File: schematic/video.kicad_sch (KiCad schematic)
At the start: 14 parts, among them J1 Conn_Coaxial, Q1 2N3904, U1 TMS4416, U14 TMS9118NL, U3 TMS4416, Y1 Crystal

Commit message: bootup works, controller waits, but no response
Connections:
- net D0: now also U14.17 (CD7); no longer U14.24 (CD0)
- net D1: now also U14.18 (CD6); no longer U14.23 (CD1)
- net D2: now also U14.19 (CD5); no longer U14.22 (CD2)
- net D3: now also U14.20 (CD4); no longer U14.21 (CD3)
- net D4: now also U14.21 (CD3); no longer U14.20 (CD4)
- net D5: now also U14.22 (CD2); no longer U14.19 (CD5)
- net D6: now also U14.23 (CD1); no longer U14.18 (CD6)
- net D7: now also U14.24 (CD0); no longer U14.17 (CD7)

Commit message: update pdf schematic and schematic wording
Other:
- title: Righteous Tentacle, Colecovision Reverse Engineering Project -> Mini Colecovision
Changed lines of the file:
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@@
   (paper "USLetter")
   (title_block
-    (title "Righteous Tentacle, Colecovision Reverse Engineering Project")
-    (date "2023-06-18")
-    (rev "1.0.0.F")
+    (title "Mini Colecovision")
+    (date "2024-03-25")
+    (rev "1.0.0")
     (company "sparkletron")
     (comment 1 "Jay Convertino")
     (comment 2 "MIT LICENSE")
-    (comment 3 "PCB: 75743 REV F")
+    (comment 3 "TARGET: Portable")
   )
   (junction (at 114.554 164.338) (diameter 0) (color 0 0 0 0)

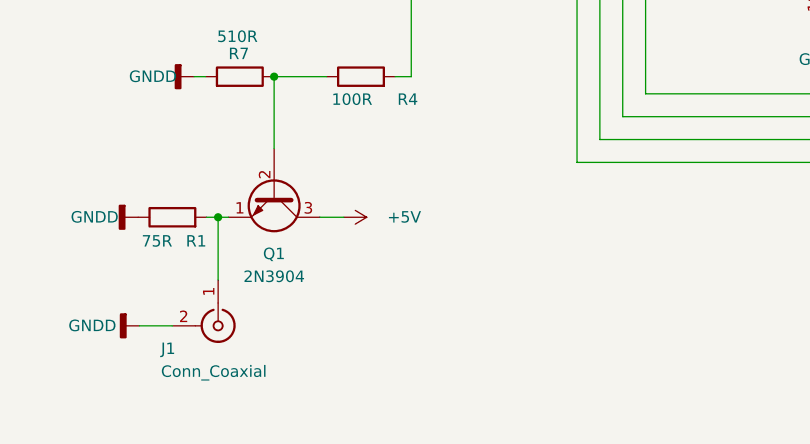
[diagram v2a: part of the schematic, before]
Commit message: first commit with PCB revised for super game module. Needs model updates and tweaks
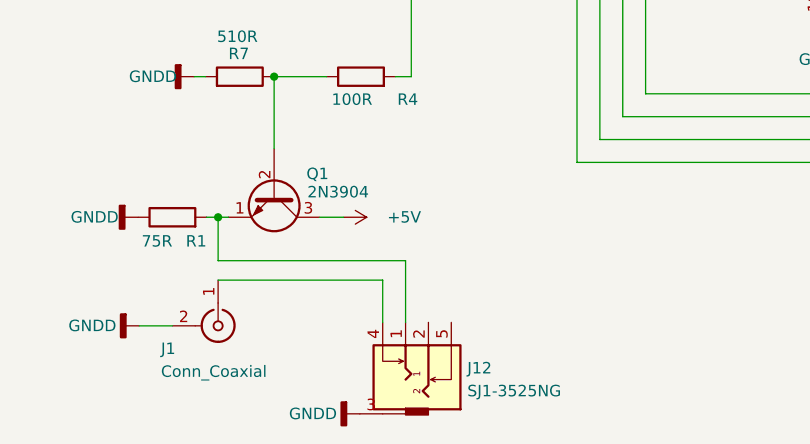
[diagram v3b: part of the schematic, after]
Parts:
- added J12: SJ1-3525NG, jacks:spc21348, symbol jacks:eighth_inch_jack
- U1, U3: footprint Package_DIP:DIP-18_W7.62mm_LongPads -> Package_DIP:DIP-18_W7.62mm
- U14: footprint Package_DIP:DIP-40_W15.24mm_LongPads -> Package_DIP:DIP-40_W15.24mm
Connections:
- net GNDD: now also J12.3
- net at Q1.1 (E), R1.2: now also J12.1; no longer J1.1 (In)
- new net: J1.1 (In), J12.4
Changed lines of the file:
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@@
     (comment 3 "TARGET: Portable")
   )
+  (junction (at 53.975 90.043) (diameter 0) (color 0 0 0 0)
+  )
+  (junction (at 53.975 97.663) (diameter 0) (color 0 0 0 0)
+  )
   (junction (at 114.554 164.338) (diameter 0) (color 0 0 0 0)
-  )
-  (junction (at 53.975 90.043) (diameter 0) (color 0 0 0 0)
-  )
-  (junction (at 53.975 97.663) (diameter 0) (color 0 0 0 0)
   )
   (junction (at 42.545 90.043) (diameter 0) (color 0 0 0 0)
@@
     (stroke (width 0) (type default))
   )
-  (wire (pts (xy 114.554 164.338) (xy 114.554 171.323))
-    (stroke (width 0) (type default))
-  )
   (wire (pts (xy 120.777 148.717) (xy 120.777 156.718))
     (stroke (width 0) (type default))
@@
     (stroke (width 0) (type default))
   )
+  (wire (pts (xy 114.554 164.338) (xy 115.697 164.338))
+    (stroke (width 0) (type default))
+  )
   (bus (pts (xy 198.247 73.787) (xy 198.247 76.327))
     (stroke (width 0) (type default))
@@
     (stroke (width 0) (type default))
   )
-  (wire (pts (xy 114.554 164.338) (xy 115.697 164.338))
-    (stroke (width 0) (type default))
-  )
   (wire (pts (xy 136.017 62.992) (xy 162.052 62.992))
     (stroke (width 0) (type default))
@@
     (stroke (width 0) (type default))
   )
+  (wire (pts (xy 135.382 169.164) (xy 135.382 176.022))
+    (stroke (width 0) (type default))
+  )
   (wire (pts (xy 136.017 112.522) (xy 159.512 112.522))
     (stroke (width 0) (type default))
   )
+  (wire (pts (xy 114.554 164.338) (xy 114.554 169.164))
+    (stroke (width 0) (type default))
+  )
   (bus (pts (xy 141.097 82.042) (xy 141.097 84.582))
     (stroke (width 0) (type default))
@@
     (stroke (width 0) (type default))
   )
+  (wire (pts (xy 114.554 169.164) (xy 135.382 169.164))
+    (stroke (width 0) (type default))
+  )
   (wire (pts (xy 193.802 150.622) (xy 193.802 137.922))
     (stroke (width 0) (type default))
@@
     (stroke (width 0) (type default))
   )
+  (wire (pts (xy 132.842 171.323) (xy 132.842 176.022))
+    (stroke (width 0) (type default))
+  )
   (wire (pts (xy 105.537 116.332) (xy 105.537 117.602))
     (stroke (width 0) (type default))
@@
   )
   (wire (pts (xy 92.837 108.712) (xy 92.837 112.522))
+    (stroke (width 0) (type default))
+  )
+  (wire (pts (xy 132.842 171.323) (xy 114.554 171.323))
     (stroke (width 0) (type default))
   )
@@
     (effects (font (size 1.27 1.27)) (justify left))
   )
+  (symbol (lib_id "jacks:eighth_inch_jack") (at 130.302 182.372 270) (mirror x) (unit 1)
+    (in_bom yes) (on_board yes) (dnp no) (fields_autoplaced)
+    (property "Reference" "J12" (at 142.24 181.102 90)
+      (effects (font (size 1.27 1.27)) (justify left))
+    )
+    (property "Value" "SJ1-3525NG" (at 142.24 183.642 90)
+      (effects (font (size 1.27 1.27)) (justify left))
+    )
+    (property "Footprint" "jacks:spc21348" (at 130.302 182.372 0)
+      (effects (font (size 1.27 1.27)) hide)
+    )
+    (property "Datasheet" "" (at 130.302 182.372 0)
+      (effects (font (size 1.27 1.27)) hide)
+    )
+    (pin "2")
+    (pin "5")
+    (pin "4")
+    (pin "3")
+    (pin "1")
+    (instances
+      (project "coleco_original"
+        (path "/970e0f64-111f-41e3-9f5a-fb0d0f6fa101/00000000-0000-0000-0000-00006262475e"
+          (reference "J12") (unit 1)
+        )
+      )
+    )
+  )
   (symbol (lib_id "Transistor_BJT:2N3904") (at 120.777 161.798 270) (unit 1)
-    (in_bom yes) (on_board yes) (dnp no) (fields_autoplaced)
-    (property "Reference" "Q1" (at 120.777 168.402 90)
+    (in_bom yes) (on_board yes) (dnp no)
+    (property "Reference" "Q1" (at 125.603 159.512 90)
       (effects (font (size 1.27 1.27)))
     )
-    (property "Value" "2N3904" (at 120.777 170.942 90)
+    (property "Value" "2N3904" (at 127.889 161.544 90)
       (effects (font (size 1.27 1.27)))
     )
@@
       (effects (font (size 1.27 1.27)) (justify left))
     )
-    (property "Footprint" "Package_DIP:DIP-40_W15.24mm_LongPads" (at 123.317 60.452 0)
+    (property "Footprint" "Package_DIP:DIP-40_W15.24mm" (at 123.317 60.452 0)
       (effects (font (size 1.27 1.27)) hide)
     )
@@
     )
   )
+  (symbol (lib_id "power:GNDD") (at 130.302 186.182 270) (unit 1)
+    (in_bom yes) (on_board yes) (dnp no) (fields_autoplaced)
+    (property "Reference" "#PWR085" (at 123.952 186.182 0)
+      (effects (font (size 1.27 1.27)) hide)
+    )
+    (property "Value" "GNDD" (at 127.762 186.182 90)
+      (effects (font (size 1.27 1.27)) (justify right))
+    )
+    (property "Footprint" "" (at 130.302 186.182 0)
+      (effects (font (size 1.27 1.27)) hide)
+    )
+    (property "Datasheet" "" (at 130.302 186.182 0)
+      (effects (font (size 1.27 1.27)) hide)
+    )
+    (pin "1")
+    (instances
+      (project "coleco_original"
+        (path "/970e0f64-111f-41e3-9f5a-fb0d0f6fa101/00000000-0000-0000-0000-00006262475e"
+          (reference "#PWR085") (unit 1)
+        )
+      )
+    )
+  )
   (symbol (lib_id "Device:R") (at 109.474 164.338 90) (unit 1)
     (in_bom yes) (on_board yes) (dnp no)
@@
       (effects (font (size 1.27 1.27)) (justify left))
     )
-    (property "Footprint" "Package_DIP:DIP-18_W7.62mm_LongPads" (at 181.737 103.632 0)
+    (property "Footprint" "Package_DIP:DIP-18_W7.62mm" (at 181.737 103.632 0)
       (effects (font (size 1.27 1.27)) hide)
     )
@@
       (effects (font (size 1.27 1.27)) (justify left))
     )
-    (property "Footprint" "Package_DIP:DIP-18_W7.62mm_LongPads" (at 181.737 72.517 0)
-      (effects (font (size 1.27 1.27)) hide)
-    )
+    (property "Footprint" "Package_DIP:DIP-18_W7.62mm" (at 181.737 72.517 0)
+      (effects (font (size 1.27 1.27)) hide)
+    )

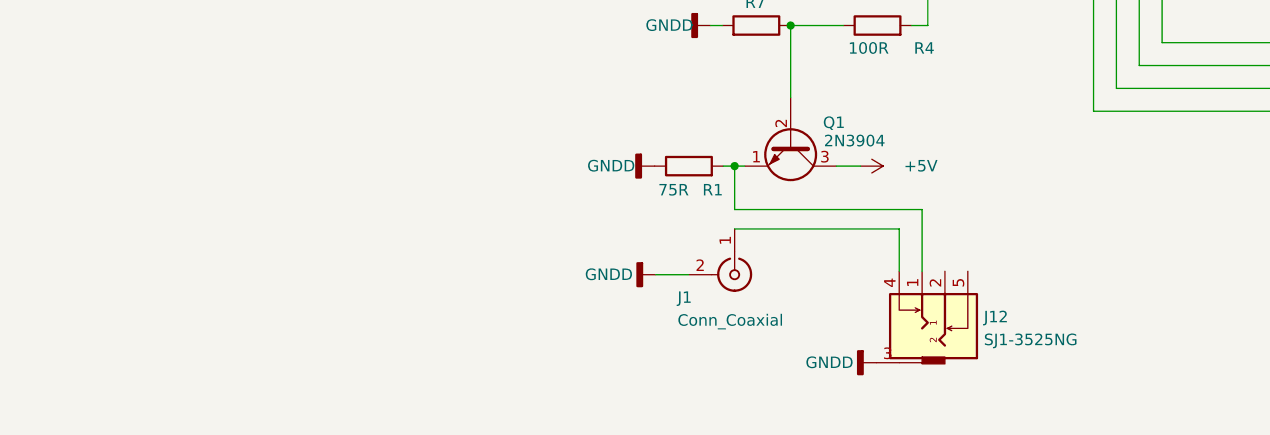
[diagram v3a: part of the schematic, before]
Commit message: updated output jacks to correct footprint
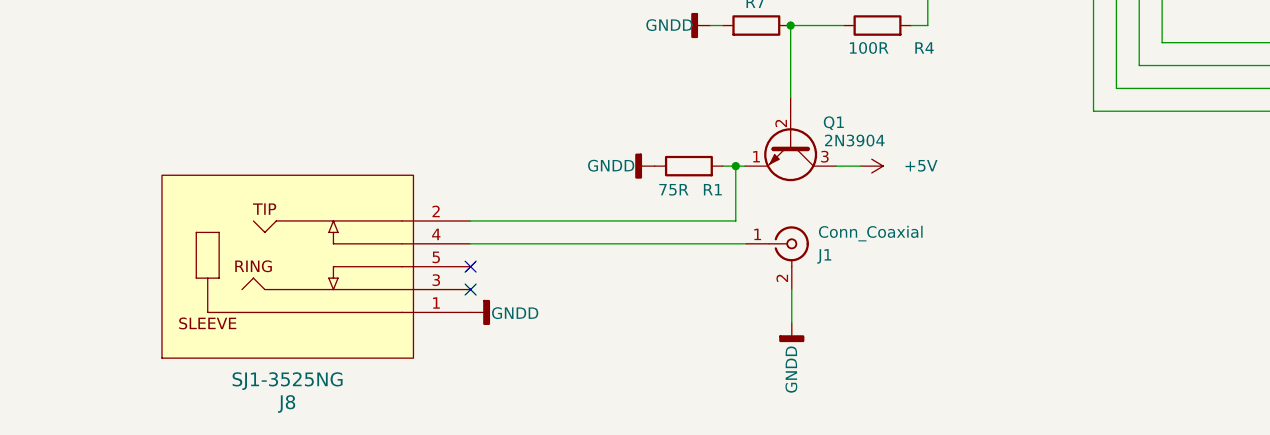
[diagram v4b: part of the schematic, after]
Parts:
- removed J12: SJ1-3525NG, jacks:spc21348, symbol jacks:eighth_inch_jack
- added J8: SJ1-3525NG, jacks2:SJ1-3525NG_CUD, symbol SJ-63053A:SJ1-3525NG
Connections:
- net GNDD: now also J8.1
- net at Q1.1 (E), R1.2: now also J8.2
- net at J1.1 (In): now also J8.4
- no-connect marks 2 -> 4
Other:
- moved on the sheet: J1
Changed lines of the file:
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@@
   (junction (at 53.975 97.663) (diameter 0) (color 0 0 0 0)
   )
-  (junction (at 114.554 164.338) (diameter 0) (color 0 0 0 0)
-  )
   (junction (at 42.545 90.043) (diameter 0) (color 0 0 0 0)
   )
@@
   (junction (at 164.592 98.552) (diameter 0) (color 0 0 0 0)
   )
+  (junction (at 114.681 164.338) (diameter 0) (color 0 0 0 0)
+  )
   (junction (at 105.537 117.602) (diameter 0) (color 0 0 0 0)
   )
@@
   (junction (at 198.247 87.122) (diameter 0) (color 0 0 0 0)
   )
+  (no_connect (at 85.217 175.514))
   (no_connect (at 136.017 122.682))
   (no_connect (at 110.617 122.682))
+  (no_connect (at 85.217 178.054))
   (bus_entry (at 195.707 104.902) (size 2.54 -2.54)
     (stroke (width 0) (type default))
@@
     (stroke (width 0) (type default))
   )
-  (wire (pts (xy 113.284 164.338) (xy 114.554 164.338))
-    (stroke (width 0) (type default))
-  )
-  (wire (pts (xy 114.554 164.338) (xy 115.697 164.338))
+  (wire (pts (xy 113.284 164.338) (xy 114.681 164.338))
     (stroke (width 0) (type default))
   )
@@
     (stroke (width 0) (type default))
   )
+  (wire (pts (xy 114.681 164.338) (xy 115.697 164.338))
+    (stroke (width 0) (type default))
+  )
   (bus (pts (xy 198.247 99.822) (xy 198.247 102.362))
     (stroke (width 0) (type default))
@@
     (stroke (width 0) (type default))
   )
-  (wire (pts (xy 135.382 169.164) (xy 135.382 176.022))
-    (stroke (width 0) (type default))
-  )
   (wire (pts (xy 136.017 112.522) (xy 159.512 112.522))
     (stroke (width 0) (type default))
   )
-  (wire (pts (xy 114.554 164.338) (xy 114.554 169.164))
+  (wire (pts (xy 114.681 164.338) (xy 114.681 170.434))
     (stroke (width 0) (type default))
   )
@@
     (stroke (width 0) (type default))
   )
-  (wire (pts (xy 114.554 169.164) (xy 135.382 169.164))
+  (wire (pts (xy 85.217 170.434) (xy 114.681 170.434))
     (stroke (width 0) (type default))
   )
@@
     (stroke (width 0) (type default))
   )
-  (wire (pts (xy 132.842 171.323) (xy 132.842 176.022))
-    (stroke (width 0) (type default))
-  )
   (wire (pts (xy 105.537 116.332) (xy 105.537 117.602))
     (stroke (width 0) (type default))
@@
     (stroke (width 0) (type default))
   )
+  (wire (pts (xy 85.217 172.974) (xy 115.824 172.974))
+    (stroke (width 0) (type default))
+  )
   (wire (pts (xy 134.239 148.717) (xy 136.017 148.717))
     (stroke (width 0) (type default))
@@
     (stroke (width 0) (type default))
   )
-  (wire (pts (xy 132.842 171.323) (xy 114.554 171.323))
-    (stroke (width 0) (type default))
-  )
   (wire (pts (xy 195.707 38.227) (xy 191.897 38.227))
     (stroke (width 0) (type default))
@@
     (stroke (width 0) (type default))
   )
-  (wire (pts (xy 105.791 176.403) (xy 109.474 176.403))
+  (wire (pts (xy 120.904 181.737) (xy 120.904 178.054))
     (stroke (width 0) (type default))
   )
@@
   (hierarchical_label "CLK" (shape output) (at 139.827 125.222 0) (fields_autoplaced)
     (effects (font (size 1.27 1.27)) (justify left))
-  )
-  (symbol (lib_id "jacks:eighth_inch_jack") (at 130.302 182.372 270) (mirror x) (unit 1)
-    (in_bom yes) (on_board yes) (dnp no) (fields_autoplaced)
-    (property "Reference" "J12" (at 142.24 181.102 90)
-      (effects (font (size 1.27 1.27)) (justify left))
-    )
-    (property "Value" "SJ1-3525NG" (at 142.24 183.642 90)
-      (effects (font (size 1.27 1.27)) (justify left))
-    )
-    (property "Footprint" "jacks:spc21348" (at 130.302 182.372 0)
-      (effects (font (size 1.27 1.27)) hide)
-    )
-    (property "Datasheet" "" (at 130.302 182.372 0)
-      (effects (font (size 1.27 1.27)) hide)
-    )
-    (pin "2")
-    (pin "5")
-    (pin "4")
-    (pin "3")
-    (pin "1")
-    (instances
-      (project "coleco_original"
-        (path "/970e0f64-111f-41e3-9f5a-fb0d0f6fa101/00000000-0000-0000-0000-00006262475e"
-          (reference "J12") (unit 1)
-        )
-      )
-    )
   )
   (symbol (lib_id "Transistor_BJT:2N3904") (at 120.777 161.798 270) (unit 1)
@@
     )
   )
-  (symbol (lib_id "power:GNDD") (at 130.302 186.182 270) (unit 1)
-    (in_bom yes) (on_board yes) (dnp no) (fields_autoplaced)
-    (property "Reference" "#PWR085" (at 123.952 186.182 0)
-      (effects (font (size 1.27 1.27)) hide)
-    )
-    (property "Value" "GNDD" (at 127.762 186.182 90)
+  (symbol (lib_id "power:GNDD") (at 85.217 180.594 90) (mirror x) (unit 1)
+    (in_bom yes) (on_board yes) (dnp no)
+    (property "Reference" "#PWR085" (at 91.567 180.594 0)
+      (effects (font (size 1.27 1.27)) hide)
+    )
+    (property "Value" "GNDD" (at 87.503 180.721 90)
       (effects (font (size 1.27 1.27)) (justify right))
     )
-    (property "Footprint" "" (at 130.302 186.182 0)
-      (effects (font (size 1.27 1.27)) hide)
-    )
-    (property "Datasheet" "" (at 130.302 186.182 0)
+    (property "Footprint" "" (at 85.217 180.594 0)
+      (effects (font (size 1.27 1.27)) hide)
+    )
+    (property "Datasheet" "" (at 85.217 180.594 0)
       (effects (font (size 1.27 1.27)) hide)
     )
@@
     )
   )
+  (symbol (lib_id "SJ-63053A:SJ1-3525NG") (at 85.217 180.594 0) (mirror x) (unit 1)
+    (in_bom yes) (on_board yes) (dnp no) (fields_autoplaced)
+    (property "Reference" "J8" (at 64.897 190.627 0)
+      (effects (font (size 1.524 1.524)))
+    )
+    (property "Value" "SJ1-3525NG" (at 64.897 188.087 0)
+      (effects (font (size 1.524 1.524)))
+    )
+    (property "Footprint" "jacks2:SJ1-3525NG_CUD" (at 85.217 180.594 0)
+      (effects (font (size 1.27 1.27) italic) hide)
+    )
+    (property "Datasheet" "SJ1-3525NG" (at 85.217 180.594 0)
+      (effects (font (size 1.27 1.27) italic) hide)
+    )
+    (pin "2")
+    (pin "3")
+    (pin "5")
+    (pin "4")
+    (pin "1")
+    (instances
+      (project "coleco_original"
+        (path "/970e0f64-111f-41e3-9f5a-fb0d0f6fa101/00000000-0000-0000-0000-00006262475e"
+          (reference "J8") (unit 1)
+        )
+      )
+    )
+  )
   (symbol (lib_id "power:GNDD") (at 105.664 164.338 270) (unit 1)
     (in_bom yes) (on_board yes) (dnp no) (fields_autoplaced)
@@
     )
   )
-  (symbol (lib_id "power:GNDD") (at 105.791 176.403 270) (unit 1)
+  (symbol (lib_id "power:GNDD") (at 120.904 181.737 0) (unit 1)
     (in_bom yes) (on_board yes) (dnp no) (fields_autoplaced)
-    (property "Reference" "#PWR038" (at 99.441 176.403 0)
-      (effects (font (size 1.27 1.27)) hide)
-    )
-    (property "Value" "GNDD" (at 103.251 176.403 90)
+    (property "Reference" "#PWR038" (at 120.904 188.087 0)
+      (effects (font (size 1.27 1.27)) hide)
+    )
+    (property "Value" "GNDD" (at 120.904 184.277 90)
       (effects (font (size 1.27 1.27)) (justify right))
     )
-    (property "Footprint" "" (at 105.791 176.403 0)
-      (effects (font (size 1.27 1.27)) hide)
-    )
-    (property "Datasheet" "" (at 105.791 176.403 0)
+    (property "Footprint" "" (at 120.904 181.737 0)
+      (effects (font (size 1.27 1.27)) hide)
+    )
+    (property "Datasheet" "" (at 120.904 181.737 0)
       (effects (font (size 1.27 1.27)) hide)
     )
@@
     )
   )
-  (symbol (lib_id "Connector:Conn_Coaxial") (at 114.554 176.403 270) (unit 1)
+  (symbol (lib_id "Connector:Conn_Coaxial") (at 120.904 172.974 0) (unit 1)
     (in_bom yes) (on_board yes) (dnp no)
-    (property "Reference" "J1" (at 108.204 178.943 90)
-      (effects (font (size 1.27 1.27)) (justify left))
-    )
-    (property "Value" "Conn_Coaxial" (at 108.204 181.483 90)
-      (effects (font (size 1.27 1.27)) (justify left))
-    )
-    (property "Footprint" "Connector_Molex:Molex_KK-254_AE-6410-02A_1x02_P2.54mm_Vertical" (at 114.554 176.403 0)
-      (effects (font (size 1.27 1.27)) hide)
-    )
-    (property "Datasheet" " ~" (at 114.554 176.403 0)
-      (effects (font (size 1.27 1.27)) hide)
-    )
+    (property "Reference" "J1" (at 123.825 174.244 0)
+      (effects (font (size 1.27 1.27)) (justify left))
+    )
+    (property "Value" "Conn_Coaxial" (at 123.825 171.704 0)
+      (effects (font (size 1.27 1.27)) (justify left))
+    )
+    (property "Footprint" "Connector_Molex:Molex_KK-254_AE-6410-02A_1x02_P2.54mm_Vertical" (at 120.904 172.974 0)
+      (effects (font (size 1.27 1.27)) hide)
+    )
+    (property "Datasheet" " ~" (at 120.904 172.974 0)
+      (effects (font (size 1.27 1.27)) hide)
+    )
